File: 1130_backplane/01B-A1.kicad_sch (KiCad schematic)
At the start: 86 parts

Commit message: Finish page KG201-KG111
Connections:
- net +ADD_TO_STORAGE_OP: now also J334.a8 (Pin_a8)
- net +BSI_E: now also J333.b4 (Pin_b4)
- net +E1_CYCLE: now also J334.b4 (Pin_b4)
- net +E2_CYCLE: now also J334.a9 (Pin_a9)
- net +FORMAT_5: now also J334.b9 (Pin_b9)
- net +I1_CYCLE: now also J334.b6 (Pin_b6)
- net +IA_CYCLE: now also J334.b8 (Pin_b8)
- net +MDX: now also J333.b10 (Pin_b10)
- net +T7_PWR: now also J334.a6 (Pin_a6)
- net +T_2: now also J333.a12 (Pin_a12)
- net +T_3: now also J333.b3 (Pin_b3)
- net +T_5: now also J333.b6 (Pin_b6)
- net +XIO_E2_R_W: now also J334.b3 (Pin_b3)
- net -ADD_TO_STOR_INTLK: now also J333.a3 (Pin_a3)
- net -BRANCH_2: now also J333.a4 (Pin_a4)
- net -E_CYCLES: now also J334.a3 (Pin_a3)
- net -INTERRUPT_REQUEST: now also J334.a7 (Pin_a7)
- net -SKIP_SAMPLE: now also J333.b9 (Pin_b9)
- net -T_4: now also J333.a8 (Pin_a8)
- net -T_6: now also J333.b11 (Pin_b11)
- net -T_7: now also J334.b10 (Pin_b10)
- net +T7_COUNT_0: now reaches J334.a1 (Pin_a1)
- net +LIKE_SIGNS: now reaches J334.a11 (Pin_a11)
- net -INC_IAR_SAMPLE: now reaches J334.a12 (Pin_a12)
- net -INC_IAR_SAMPLE: now also J339.b6 (Pin_b6)
- net -A_TO_M_SPD_GATE: now reaches J334.a4 (Pin_a4)
- net -A_TO_M_SPD_GATE: now also J340.b1 (Pin_b1)
- net +LOAD_IAR_KEY: now reaches J334.b1 (Pin_b1)
- net +LOAD_IAR_KEY: now also J262.b1 (Pin_b1)
- net -A_REG_EQUAL_ZERO: now reaches J334.b11 (Pin_b11)
- net -I_TO_M_SPD_GATE: now reaches J334.b5 (Pin_b5)
- net -I_TO_M_SPD_GATE: now also J340.b8 (Pin_b8)
- net -IAR_0-7_INCR_GT: now reaches J339.a2 (Pin_a2)
- net -IAR_0-7_INCR_GT: now also J333.b1 (Pin_b1)
- net -M_TO_I_SPD_GATE: now reaches J339.b1 (Pin_b1)
- net -M_TO_I_SPD_GATE: now also J333.a2 (Pin_a2)
- net -IAR_8-15_INCR_GT: now reaches J339.b2 (Pin_b2)
- net -IAR_8-15_INCR_GT: now also J333.a1 (Pin_a1)
- net -B_TO_I_GATE: now reaches J339.b5 (Pin_b5)
- net -B_TO_I_GATE: now also J333.b5 (Pin_b5)
- net -I_CYCLE_INCR_IAR_SAMPLE: now reaches J333.a11 (Pin_a11)
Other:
- note added: "5804610"
- note added: "5804625"

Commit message: Finish page KG221-KG151
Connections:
- net +3V: no longer J342.b2 (Pin_b2)
- net +6V: no longer J342.a10 (Pin_a10)
- net +ADD_TO_STORAGE_OP: now also J328.b6 (Pin_b6), J335.b9 (Pin_b9)
- net +BRANCH_2: now also J336.a3 (Pin_a3)
- net +DBL_WORD_ADDRESSING: now also J327.a11 (Pin_a11)
- net +DIVIDE_OP: now also J284.a3 (Pin_a3)
- net +E1_CYCLE: now also J283.a11 (Pin_a11), J328.b1 (Pin_b1), J335.b10 (Pin_b10)
- net +E2_CYCLE: now also J327.b10 (Pin_b10)
- net +E_CYCLES: now also J283.b11 (Pin_b11), J327.b1 (Pin_b1)
- net +I1_POWERED: now also J284.b1 (Pin_b1), J335.b5 (Pin_b5)
- net +I1_T3: now also J336.a12 (Pin_a12)
- net +IA_CYCLE: now also J328.b9 (Pin_b9)
- net +MDX: now also J328.a12 (Pin_a12)
- net +MULTIPLY_OP: now also J284.a4 (Pin_a4)
- net +PHASE_A: now also J328.a11 (Pin_a11)
- net +PHASE_B: now also J328.b8 (Pin_b8)
- net +SHIFT_INSTR: now also J283.b4 (Pin_b4), J336.b10 (Pin_b10)
- net +STX_OP: now also J327.b4 (Pin_b4), J335.a3 (Pin_a3)
- net +T7_COUNT_0: now also J284.a9 (Pin_a9)
- net +TAG_00: now also J327.b3 (Pin_b3), J335.a8 (Pin_a8)
- net +T_1: now also J283.b6 (Pin_b6), J336.b8 (Pin_b8)
- net +T_2: now also J327.a4 (Pin_a4), J335.b6 (Pin_b6)
- net +T_5: now also J284.b3 (Pin_b3)
- net +T_6: now also J336.b12 (Pin_b12)
- net +T_7: now also J284.b8 (Pin_b8)
- net +XIO_E1: now also J336.b11 (Pin_b11)
- net -3V: no longer J342.a5 (Pin_a5)
- net -ARITH_CTRL_A: now also J283.b12 (Pin_b12)
- net -A_REG_EQUAL_ZERO: now also J283.b1 (Pin_b1)
- net -BR-2_NOT_BR-1_RESET_CCC: now also J283.a4 (Pin_a4)
- net -BSI_E: now also J327.a1 (Pin_a1)
- net -BSI_TRUE_OR_BSC_TRUE: now also J284.b9 (Pin_b9), J336.b4 (Pin_b4)
- net -CCC_DECREM_SAMPLE: now also J283.a12 (Pin_a12)
- net -DBL_WORD_ADDRESSING: now also J283.b9 (Pin_b9)
- net -DC_RESET_1: now also J283.a2 (Pin_a2), J328.a3 (Pin_a3)
- net -DIVIDE_OP: now also J284.b10 (Pin_b10)
- net -E_CYCLES: now also J283.b3 (Pin_b3)
- net -I1_CYCLE: now also J328.a8 (Pin_a8), J336.b1 (Pin_b1)
- net -INDEX_INSTR: now also J283.b10 (Pin_b10), J336.b6 (Pin_b6)
- net -LDX_OP: now also J283.b8 (Pin_b8), J327.a12 (Pin_a12), J335.a7 (Pin_a7)
- net -LOAD_DISPLAY_PROGRAM_LOAD: now also J335.a6 (Pin_a6)
- net -MDX_OP: now also J327.a9 (Pin_a9)
- net -MULTIPLY_OP: now also J283.a9 (Pin_a9)
- net -OP_001X0: now also J284.b5 (Pin_b5), J336.b5 (Pin_b5)
- net -SHIFT_INSTR: now also J283.a6 (Pin_a6), J335.b4 (Pin_b4), J336.a9 (Pin_a9)
- net -STORE_E: now also J327.b8 (Pin_b8)
- net -STORE_STATUS_E: now also J327.b9 (Pin_b9), J336.b3 (Pin_b3)
- net -T7_COUNT_0: now also J284.a12 (Pin_a12)
- net -T_7: now also J328.a2 (Pin_a2)
- net -XIO_E2_R_W: now also J283.a8 (Pin_a8)
- net +GATE_I_TO_A_0-7: now reaches J339.a3 (Pin_a3)
- net +GATE_I_TO_A_0-7: now also J335.a1 (Pin_a1)
- net -A_TO_B_0-7_SPD_GATE: now reaches J339.a4 (Pin_a4)
- net -A_TO_B_0-7_SPD_GATE: now also J327.a6 (Pin_a6)
- net -I_TO_B_SPD_GATE: now reaches J339.a5 (Pin_a5)
- net -I_TO_B_SPD_GATE: now also J327.a7 (Pin_a7)
- net +GATE_I_TO_A_8-15: now reaches J339.b3 (Pin_b3)
- net +GATE_I_TO_A_8-15: now also J335.a2 (Pin_a2)
- net -A_TO_B_8-15_SPD_GATE: now reaches J339.b4 (Pin_b4)
- net -A_TO_B_8-15_SPD_GATE: now also J327.a3 (Pin_a3)
- net -DC_RESET_CCC: now reaches J283.a1 (Pin_a1)
- net +A-REG_EQUAL_0_LATCHED: now reaches J283.a3 (Pin_a3)
- net -STX_TAG_00: now reaches J283.a7 (Pin_a7)
- net -STX_TAG_00: now also J327.a2 (Pin_a2)
- net -SET_DIV_OFLO_E1_E2: now reaches J283.b5 (Pin_b5)
- net -DC_SET_D_0-7: now reaches J341.b6 (Pin_b6)
- net -DC_SET_D_0-7: now also J335.a9 (Pin_a9)
- net -SET_CCC_16: now reaches J284.a1 (Pin_a1)
- net -SET_CCC_1: now reaches J284.a11 (Pin_a11)
- net -SET_CCC_18: now reaches J284.a2 (Pin_a2)
- net -T7_NOT_COUNT_0: now reaches J284.a6 (Pin_a6)
- net -CCC_COUNT_0: now reaches J284.a7 (Pin_a7)
- net -SHIFT_OP_GATE: now reaches J284.a8 (Pin_a8)
- net +CCC_COUNT_0: now reaches J284.b11 (Pin_b11)
- net +CCC_COUNT_0: now also J335.b11 (Pin_b11)
- net +T7_END_OP: now reaches J284.b12 (Pin_b12)
- net +T7_END_OP: now also J336.a1 (Pin_a1)
- net -BSC_NOT_FORMAT: now reaches J284.b4 (Pin_b4)
- net -BSC_NOT_FORMAT: now also J336.a2 (Pin_a2)
- net -WAIT_OP: now reaches J284.b6 (Pin_b6)
- net -WAIT_OP: now also J336.a4 (Pin_a4)
- net -A_TO_U_SPD_SAMPLE: now reaches J336.a11 (Pin_a11)
- net -A_TO_U_SPD_SAMPLE: now also J342.b1 (Pin_b1)
- net -U_TO_A_SPD_SAMPLE: now reaches J336.a6 (Pin_a6)
- net -U_TO_A_SPD_SAMPLE: now also J342.a6 (Pin_a6)
- net -SLC_E: now reaches J336.a7 (Pin_a7)
- net -SLC_E: now also J327.b6 (Pin_b6)
- net +GATE_B_TO_D_0-7: now reaches J340.a4 (Pin_a4)
- net +GATE_B_TO_D_0-7: now also J335.a12 (Pin_a12)
- net +GATE_B_TO_D_8-15: now reaches J340.b4 (Pin_b4)
- net +GATE_B_TO_D_8-15: now also J335.b1 (Pin_b1)
- net -DBL_PREC_E2: now reaches J327.b11 (Pin_b11)
- net +DBL_PREC_E2: now reaches J327.b12 (Pin_b12)
- net +DIVIDE_E: now reaches J335.a11 (Pin_a11)
- net -B_BIT_8_TO_D: now reaches J335.b3 (Pin_b3)
- net +MULT_OP_E: now reaches J328.a1 (Pin_a1)
- net -T3_PHASE_B: now reaches J328.a4 (Pin_a4)
- net +WRITE_GATE_PHASE_B: now reaches J328.a6 (Pin_a6)
- net +ADD_SUB_GT_E: now reaches J328.a7 (Pin_a7)
- net -B_BIT_0_LATCHED: now reaches J328.a9 (Pin_a9)
- net +DIVIDE_E1: now reaches J328.b10 (Pin_b10)
- net +B_BIT_0_LATCHED: now reaches J328.b11 (Pin_b11)
- net +WRITE_GATE_PHASE_A: now reaches J328.b12 (Pin_b12)
- net -CLOCK_ADVANCE_SP_A: now reaches J328.b3 (Pin_b3)
- net -B_BIT_0_TO_D: now reaches J328.b4 (Pin_b4)
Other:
- note added: "5804621"
- note added: "5804624"
- note added: "CABL 01B-B1A5"

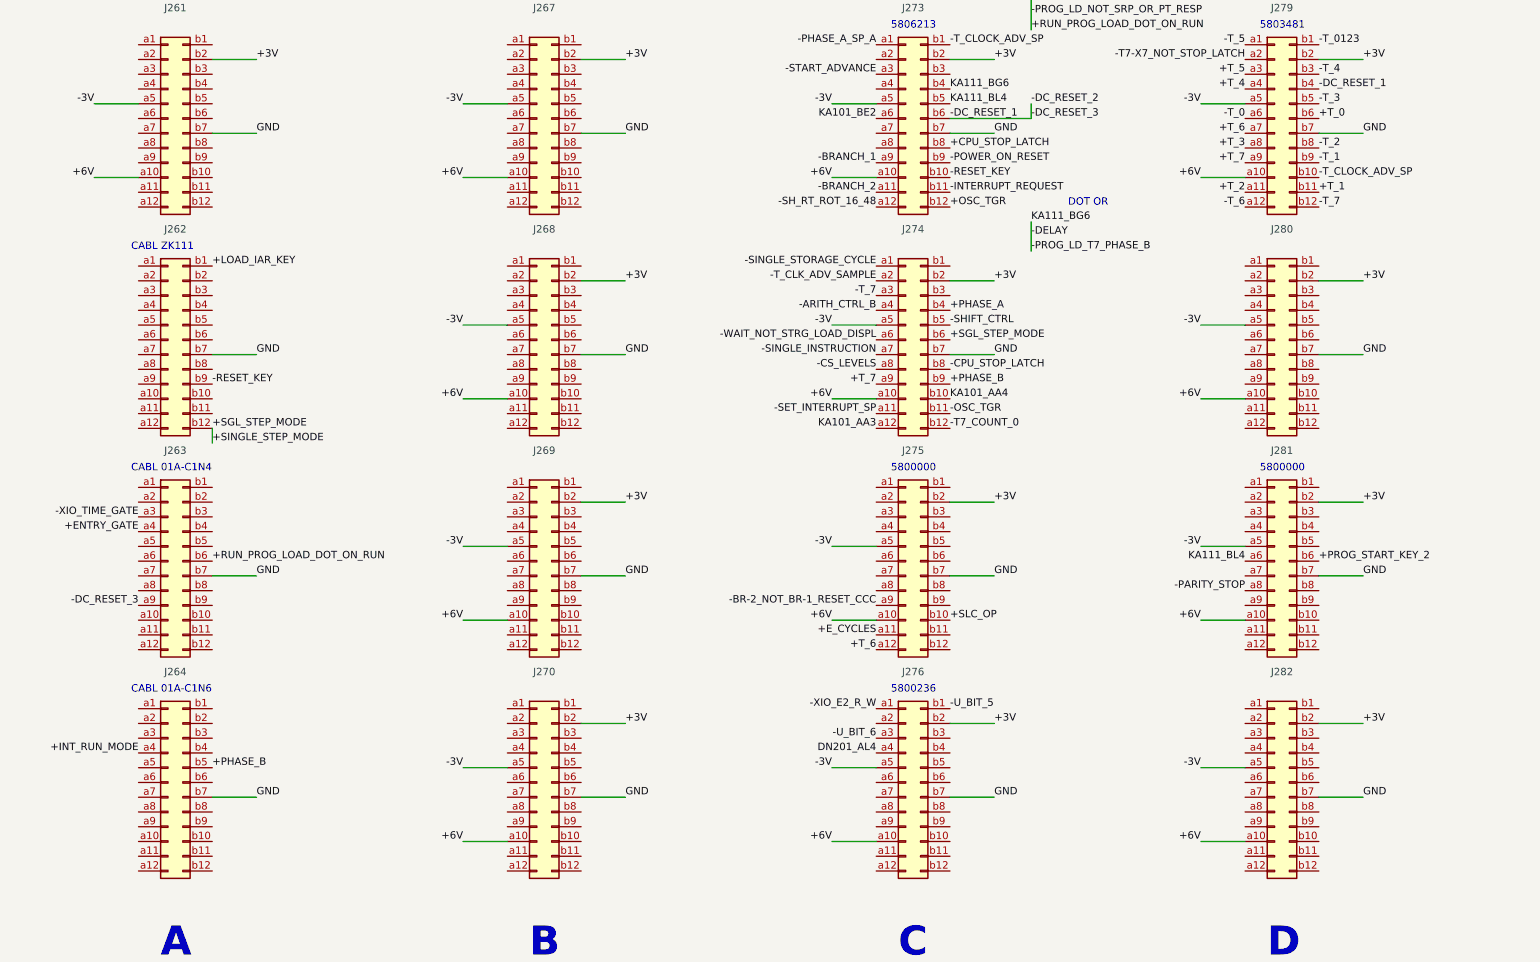
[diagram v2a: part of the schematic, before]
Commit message: Finish page KM101-KM111
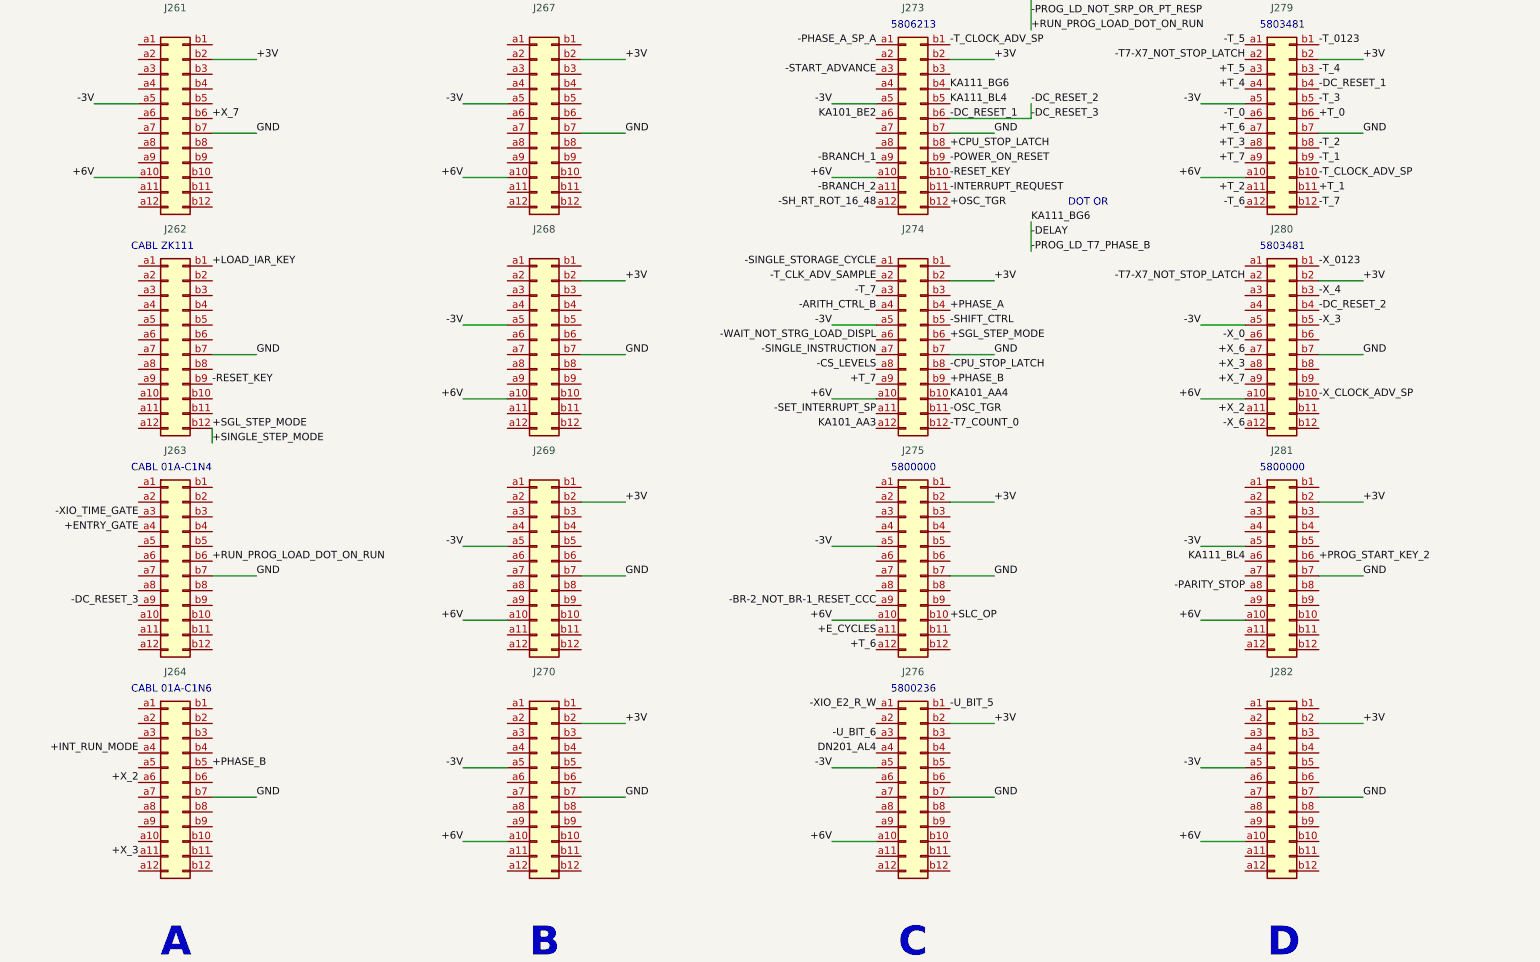
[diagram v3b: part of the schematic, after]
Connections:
- net -DC_RESET_1: now also J280.b4 (Pin_b4)
- net -T7-X7_NOT_STOP_LATCH: now also J280.a2 (Pin_a2)
- net +X_2: now reaches J280.a11 (Pin_a11)
- net +X_2: now also J264.a6 (Pin_a6)
- net -X_6: now reaches J280.a12 (Pin_a12)
- net -X_0: now reaches J280.a6 (Pin_a6)
- net +X_6: now reaches J280.a7 (Pin_a7)
- net +X_3: now reaches J280.a8 (Pin_a8)
- net +X_3: now also J264.a11 (Pin_a11)
- net +X_7: now reaches J280.a9 (Pin_a9)
- net +X_7: now also J261.b6 (Pin_b6)
- net -X_0123: now reaches J280.b1 (Pin_b1)
- net -X_CLOCK_ADV_SP: now reaches J280.b10 (Pin_b10)
- net -X_4: now reaches J280.b3 (Pin_b3)
- net -X_3: now reaches J280.b5 (Pin_b5)
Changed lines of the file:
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@@
     (effects (font (size 5 5) (thickness 1) bold) (justify left bottom))
+  )
+  (text "5803481" (at 226.06 215.9 0)
+    (effects (font (size 1.27 1.27)) (justify left bottom))
   )
   (text "B" (at 320.04 379.73 0)
@@
     (effects (font (size 1.27 1.27)) (justify right bottom))
   )
+  (label "-T7-X7_NOT_STOP_LATCH" (at 223.52 220.98 180)
+    (effects (font (size 1.27 1.27)) (justify right bottom))
+  )
   (label "-I1_CYCLE" (at 668.02 160.02 180)
     (effects (font (size 1.27 1.27)) (justify right bottom))
@@
     (effects (font (size 1.27 1.27)) (justify right bottom))
   )
+  (label "-X_6" (at 223.52 246.38 180)
+    (effects (font (size 1.27 1.27)) (justify right bottom))
+  )
   (label "DN201_AL4" (at 807.72 299.72 0)
     (effects (font (size 1.27 1.27)) (justify left bottom))
@@
     (effects (font (size 1.27 1.27)) (justify right bottom))
   )
+  (label "+X_6" (at 223.52 233.68 180)
+    (effects (font (size 1.27 1.27)) (justify right bottom))
+  )
   (label "+FORMAT_5" (at 426.72 162.56 0)
     (effects (font (size 1.27 1.27)) (justify left bottom))
@@
     (effects (font (size 1.27 1.27)) (justify right bottom))
   )
+  (label "+X_7" (at 45.72 193.04 0)
+    (effects (font (size 1.27 1.27)) (justify left bottom))
+  )
   (label "-LDX_OP" (at 731.52 195.58 180)
     (effects (font (size 1.27 1.27)) (justify right bottom))
@@
     (effects (font (size 1.27 1.27)) (justify right bottom))
   )
+  (label "+X_3" (at 223.52 236.22 180)
+    (effects (font (size 1.27 1.27)) (justify right bottom))
+  )
   (label "+3V" (at 497.84 259.08 0)
     (effects (font (size 1.27 1.27)) (justify left bottom))
@@
     (effects (font (size 1.27 1.27)) (justify left bottom))
   )
+  (label "-X_0123" (at 236.22 218.44 0)
+    (effects (font (size 1.27 1.27)) (justify left bottom))
+  )
   (label "+OP_BIT_0" (at 236.22 109.22 0)
     (effects (font (size 1.27 1.27)) (justify left bottom))
@@
     (effects (font (size 1.27 1.27)) (justify left bottom))
   )
+  (label "-X_4" (at 236.22 223.52 0)
+    (effects (font (size 1.27 1.27)) (justify left bottom))
+  )
   (label "-WAIT_NOT_STRG_LOAD_DISPL" (at 160.02 231.14 180)
     (effects (font (size 1.27 1.27)) (justify right bottom))
@@
     (effects (font (size 1.27 1.27)) (justify right bottom))
   )
+  (label "+X_7" (at 223.52 238.76 180)
+    (effects (font (size 1.27 1.27)) (justify right bottom))
+  )
   (label "-T7_NOT_COUNT_0" (at 287.02 154.94 180)
     (effects (font (size 1.27 1.27)) (justify right bottom))
@@
     (effects (font (size 1.27 1.27)) (justify right bottom))
   )
+  (label "-X_CLOCK_ADV_SP" (at 236.22 241.3 0)
+    (effects (font (size 1.27 1.27)) (justify left bottom))
+  )
   (label "+E1_CYCLE" (at 680.72 142.24 0)
     (effects (font (size 1.27 1.27)) (justify left bottom))
@@
     (effects (font (size 1.27 1.27)) (justify left bottom))
   )
+  (label "-DC_RESET_2" (at 236.22 226.06 0)
+    (effects (font (size 1.27 1.27)) (justify left bottom))
+  )
   (label "-T_CLK_ADV_SAMPLE" (at 160.02 220.98 180)
     (effects (font (size 1.27 1.27)) (justify right bottom))
@@
     (effects (font (size 1.27 1.27)) (justify left bottom))
   )
+  (label "-X_3" (at 236.22 228.6 0)
+    (effects (font (size 1.27 1.27)) (justify left bottom))
+  )
   (label "+ENTRY_GATE" (at 33.02 264.16 180)
     (effects (font (size 1.27 1.27)) (justify right bottom))
@@
     (effects (font (size 1.27 1.27)) (justify right bottom))
   )
+  (label "+X_2" (at 223.52 243.84 180)
+    (effects (font (size 1.27 1.27)) (justify right bottom))
+  )
   (label "-INTERRUPT_LVLS_0123" (at 541.02 259.08 180)
     (effects (font (size 1.27 1.27)) (justify right bottom))
@@
     (effects (font (size 1.27 1.27)) (justify right bottom))
   )
+  (label "+X_2" (at 33.02 307.34 180)
+    (effects (font (size 1.27 1.27)) (justify right bottom))
+  )
   (label "+E1_CYCLE" (at 287.02 129.54 180)
     (effects (font (size 1.27 1.27)) (justify right bottom))
@@
     (effects (font (size 1.27 1.27)) (justify left bottom))
   )
+  (label "+X_3" (at 33.02 320.04 180)
+    (effects (font (size 1.27 1.27)) (justify right bottom))
+  )
   (label "+E3_CYCLE" (at 45.72 149.86 0)
     (effects (font (size 1.27 1.27)) (justify left bottom))
@@
     (effects (font (size 1.27 1.27)) (justify left bottom))
   )
+  (label "-X_0" (at 223.52 231.14 180)
+    (effects (font (size 1.27 1.27)) (justify right bottom))
+  )
   (label "-BRANCH_2" (at 604.52 144.78 180)

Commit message: Finish page KM201-KM211
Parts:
- added JP? (x2): NO CYCLE STEAL, symbol Jumper:Jumper_2_Bridged
- added JP?: NO 1442, symbol Jumper:Jumper_2_Bridged
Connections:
- net +CCC_COUNT_0: now also J311.b1 (Pin_b1)
- net +ENTRY_GATE: now also J311.b11 (Pin_b11)
- net +I2_CYCLE: now also J311.b6 (Pin_b6)
- net +INTERRUPT_REQUEST: now also J312.b11 (Pin_b11)
- net +NOT_STORAGE_USE: now also J325.a4 (Pin_a4)
- net +PHASE_B: now also J311.a12 (Pin_a12), J325.a8 (Pin_a8)
- net +RUN_PROG_LOAD_DOT_ON_RUN: now also J325.a9 (Pin_a9)
- net +T_0: now also J312.b12 (Pin_b12)
- net +T_1: now also J325.b1 (Pin_b1)
- net +T_3: now also J275.b4 (Pin_b4), J311.b12 (Pin_b12)
- net +T_7: now also J311.b10 (Pin_b10), J325.a7 (Pin_a7)
- net +X_3: now also J276.a11 (Pin_a11)
- net +X_7: now also J311.a11 (Pin_a11)
- net -CS_LEVELS: now also J296.b1 (Pin_b1), J296.b3 (Pin_b3), J344.a1 (Pin_a1)
- net -CS_LEVEL_0: now also J264.a1 (Pin_a1), J296.a9 (Pin_a9)
- net -CS_LEVEL_1: now also J296.b11 (Pin_b11), J344.a4 (Pin_a4)
- net -DC_RESET_1: now also J296.a4 (Pin_a4)
- net -DELAY: now also J325.a6 (Pin_a6)
- net -INTERRUPT_LEVEL_5: now also J319.a4 (Pin_a4)
- net -INTERRUPT_REQUESTS_23: now also J319.b6 (Pin_b6)
- net -INTERRUPT_REQUESTS_45: now also J320.a6 (Pin_a6)
- net -SET_INTERRUPT_SP: now also J296.a8 (Pin_a8)
- net GND: now also JP?.2 (B), JP?.2 (B), JP?.2 (B)
- net KM201_AB4: now reaches J312.b9 (Pin_b9)
- net KM201_AB4: now also J320.b8 (Pin_b8)
- net +CS_LEVEL_0: now reaches J276.a12 (Pin_a12)
- net +CS_LEVEL_0: now also J296.b9 (Pin_b9), J344.a10 (Pin_a10), JP?.1 (A)
- net -I_O_ENTR_SAMPLE: now reaches J276.a9 (Pin_a9)
- net -I_O_ENTR_SAMPLE: now also J275.b3 (Pin_b3), J311.b9 (Pin_b9), J325.a1 (Pin_a1), J344.b5 (Pin_b5)
- net +FILE_DATA_ENTRY_GATE: now reaches J276.b10 (Pin_b10)
- net +PROGRAM_LOAD: now reaches J325.a11 (Pin_a11)
- net +PROGRAM_LOAD: now also J320.a11 (Pin_a11), J325.b6 (Pin_b6)
- net -PT_RESPONSE: now reaches J325.a12 (Pin_a12)
- net -LEVEL_0_RESPONSE: now reaches J325.b10 (Pin_b10)
- net -LEVEL_0_RESPONSE: now also J320.b12 (Pin_b12)
- net KM201_AF4: now reaches J311.a1 (Pin_a1)
- net KM201_AF4: now also J320.b6 (Pin_b6)
- net -PROGRAM_LOAD: now reaches J311.a3 (Pin_a3)
- net -INTERRUPT_DELAY: now reaches J311.a4 (Pin_a4)
- net KM201_AQ4: now reaches J311.a6 (Pin_a6)
- net KM201_AQ4: now also J320.b1 (Pin_b1)
- net +T6_PWR_1: now reaches J311.a8 (Pin_a8)
- net -T7_X7_PHASE_B_SAMPLE: now reaches J311.a9 (Pin_a9)
- net +LOAD: now reaches J275.a2 (Pin_a2)
- net +REQ_INTERRUPT_LVL_0: now reaches J320.a12 (Pin_a12)
- net +REQ_INTERRUPT_LVL_0: now also JP?.1 (A)
- net +I2_T6: now reaches J320.a2 (Pin_a2)
- net KM201_AS4: now reaches J320.a7 (Pin_a7)
- net KM201_AS4: now also J344.b9 (Pin_b9)
- net KM201_AL4: now reaches J320.a8 (Pin_a8)
- net KM201_AL4: now also J344.b8 (Pin_b8)
- net -PROG_LOAD: now reaches J320.a9 (Pin_a9)
- net +GATE_INTERRUPT: now reaches J320.b10 (Pin_b10)
- net KM201_AD4: now reaches J319.a1 (Pin_a1)
- net KM201_AD4: now also J344.b11 (Pin_b11)
- net -INTERRUPT_LEVEL_3: now reaches J319.a3 (Pin_a3)
- net KM201_AC4: now reaches J319.a6 (Pin_a6)
- net KM201_AC4: now also J344.b10 (Pin_b10)
- net -INTERRUPT_LEVEL_1: now reaches J319.b1 (Pin_b1)
- net -PRINTER_C_S_REQ: now reaches J344.a5 (Pin_a5)
- net -PRINTER_C_S_REQ: now also J296.b4 (Pin_b4)
- net +CS_LEVEL_1: now reaches J344.a6 (Pin_a6)
- net +CS_LEVEL_1: now also J296.b10 (Pin_b10), JP?.1 (A)
- net -REQ_C_S_LVL_0: now reaches J296.a1 (Pin_a1)
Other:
- note added: "5803815"
